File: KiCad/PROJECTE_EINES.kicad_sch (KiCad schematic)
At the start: 5 parts, among them J3 J_DEBUG

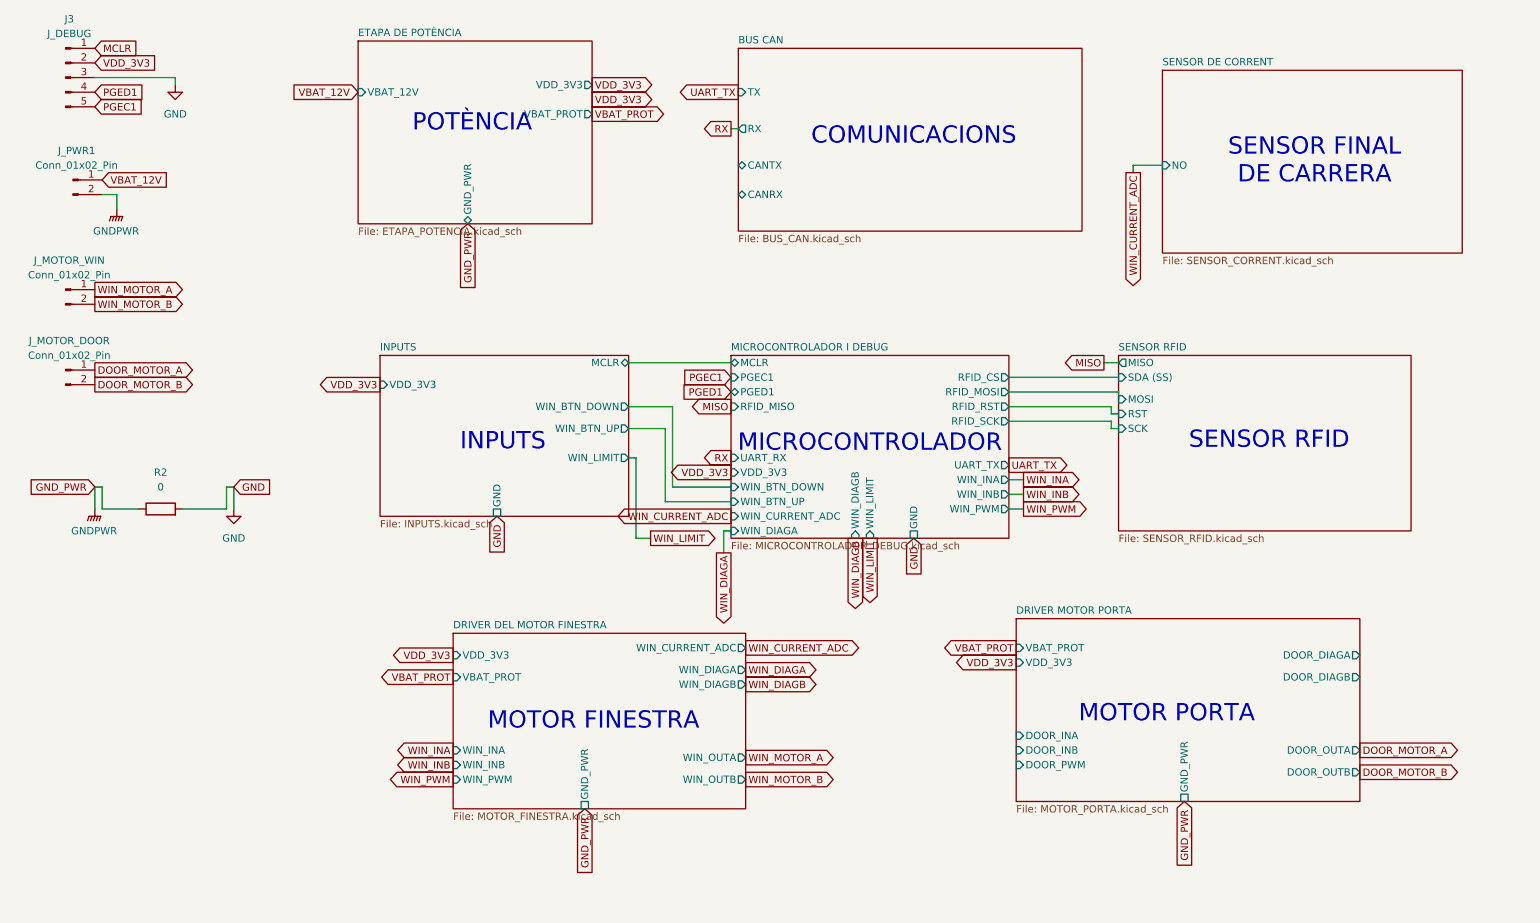
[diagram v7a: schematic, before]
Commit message: Etiquetes de GND i VCC 3.3V canviades a simbols
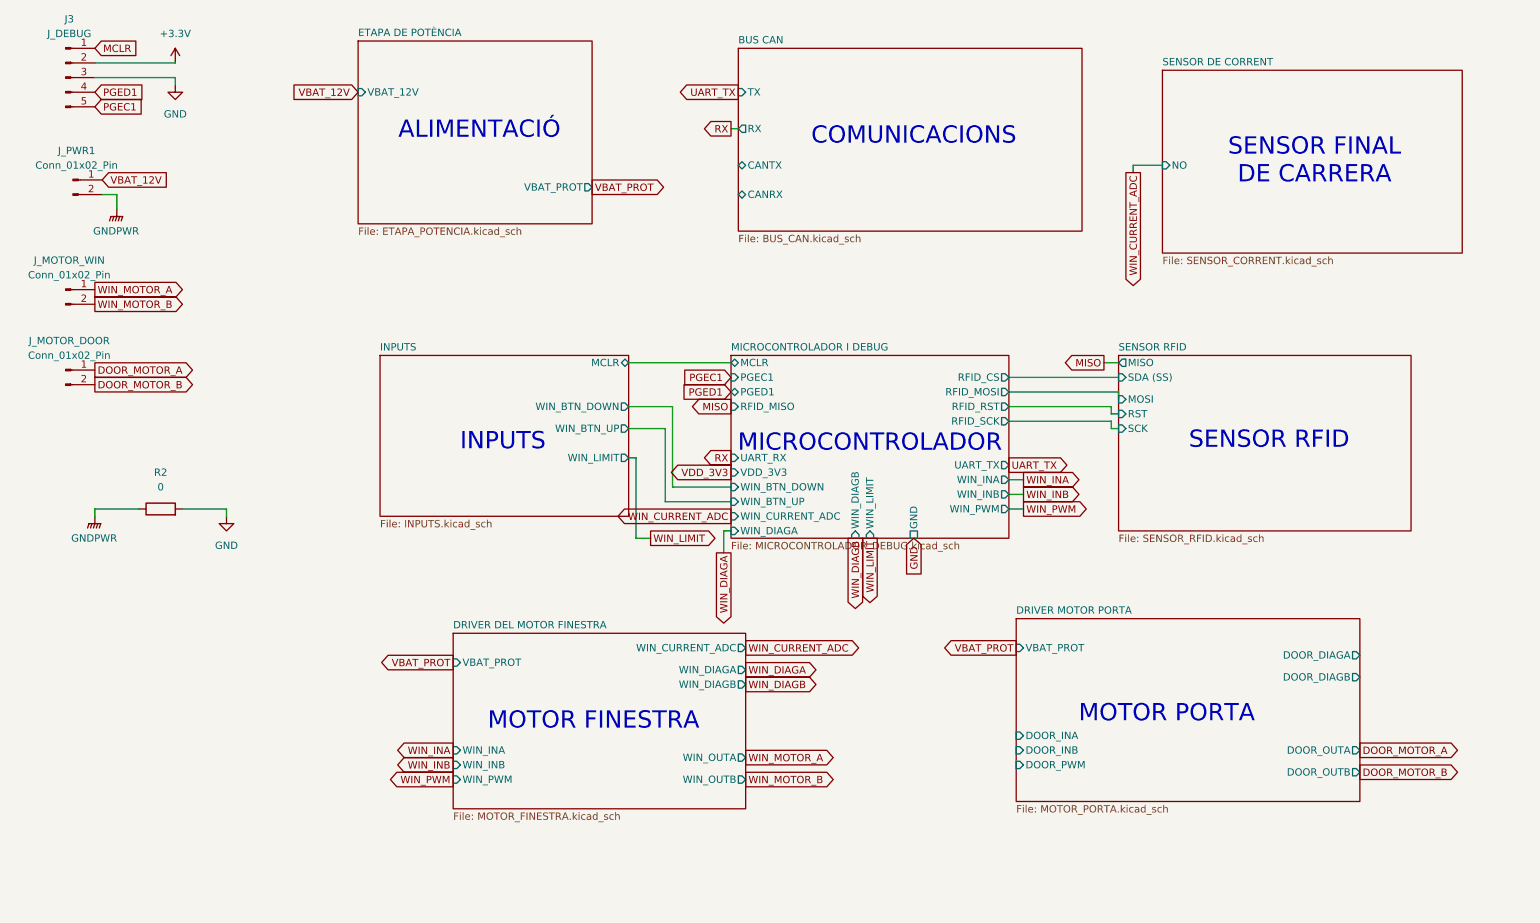
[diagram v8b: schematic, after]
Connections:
- net VDD_3V3: no longer J3.2 (Pin_2)
- new net +3.3V: J3.2 (Pin_2)
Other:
- sheet DRIVER DEL MOTOR FINESTRA ports: added none; removed GND_PWR, VDD_3V3
- sheet DRIVER MOTOR PORTA ports: added none; removed GND_PWR, VDD_3V3
- sheet ETAPA DE POTÈNCIA ports: added none; removed GND_PWR, VDD_3V3
- sheet INPUTS ports: added none; removed GND, VDD_3V3
- note added: "ALIMENTACIÓ"
- note removed: "POTÈNCIA"
